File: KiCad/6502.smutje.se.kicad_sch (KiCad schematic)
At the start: 10 parts, among them U11 W65C02S

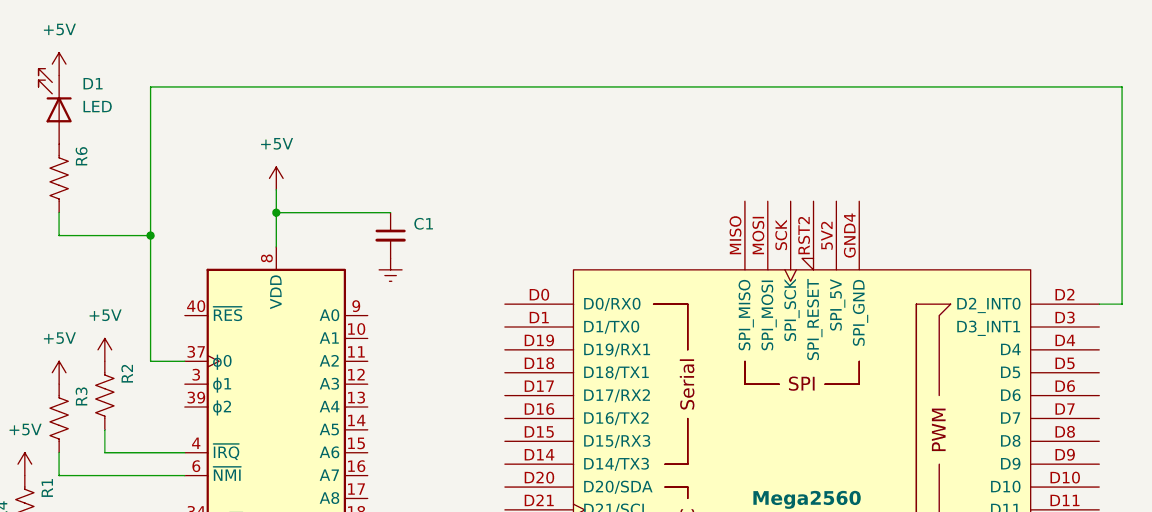
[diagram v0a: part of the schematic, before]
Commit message: Add trim potentiometer symbol and update power symbols in schematics
- Introduced a new trim potentiometer symbol (Device:R_Potentiometer_Trim) with properties for reference, value, footprint, and simulation details.
- Updated existing power symbols for +5V and Earth, including new references and descriptions.
- Adjusted positions and properties of various components in the schematic to enhance clarity and organization.
- Updated multiple schematic images to reflect the latest changes.
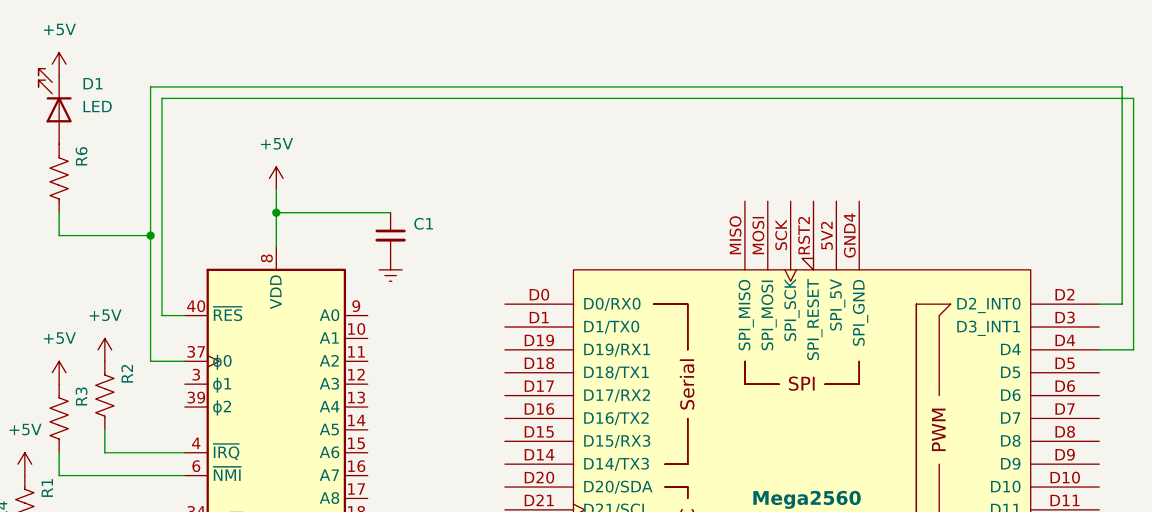
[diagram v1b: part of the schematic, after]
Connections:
- net at A5.D4: now also U11.40 (~{RES})
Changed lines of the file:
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@@
+	(wire
+		(pts
+			(xy 217.17 97.79) (xy 213.36 97.79)
+		)
+		(stroke
+			(width 0)
+			(type default)
+		)
+	)
 	(wire
 		(pts
@@
 	(wire
 		(pts
+			(xy 217.17 69.85) (xy 217.17 97.79)
+		)
+		(stroke
+			(width 0)
+			(type default)
+		)
+	)
+	(wire
+		(pts
+			(xy 111.76 93.98) (xy 109.22 93.98)
+		)
+		(stroke
+			(width 0)
+			(type default)
+		)
+	)
+	(wire
+		(pts
 			(xy 107.95 85.09) (xy 97.79 85.09)
 		)
@@
 	(wire
 		(pts
+			(xy 109.22 69.85) (xy 217.17 69.85)
+		)
+		(stroke
+			(width 0)
+			(type default)
+		)
+	)
+	(wire
+		(pts
 			(xy 97.79 109.22) (xy 97.79 111.76)
 		)
@@
 		)
 		(stroke
+			(width 0)
+			(type default)
+		)
+	)
+	(wire
+		(pts
+			(xy 109.22 93.98) (xy 109.22 69.85)
+		)
+		(stroke

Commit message: Revert "Add trim potentiometer symbol and update power symbols in schematics"
This reverts commit c4bb345892a428583a00d61d4c040ffcc3a1eb40.
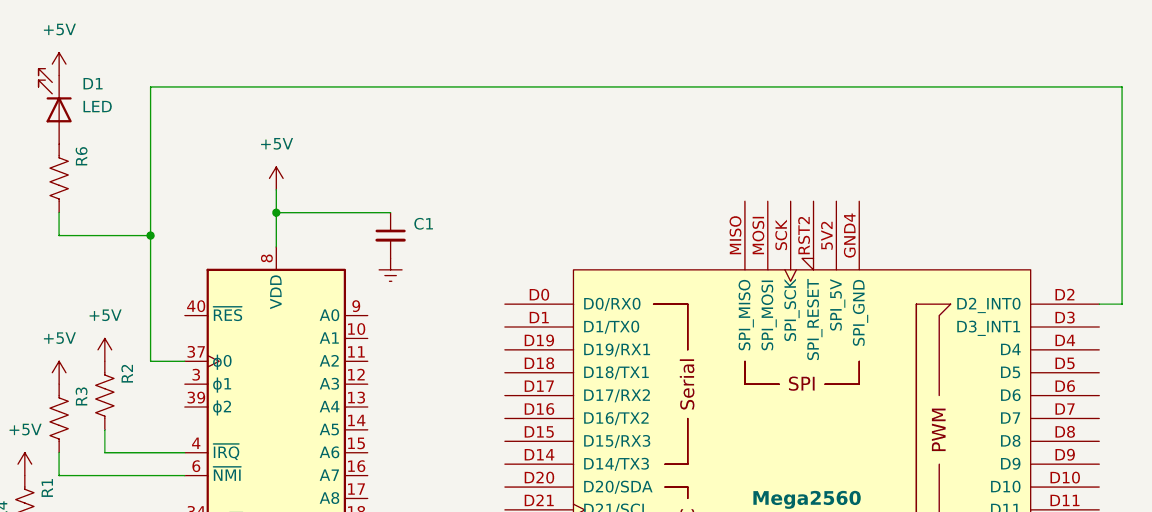
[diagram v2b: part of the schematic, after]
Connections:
- net at A5.D4: no longer U11.40 (~{RES})
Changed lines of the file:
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@@
-	(wire
-		(pts
-			(xy 217.17 97.79) (xy 213.36 97.79)
-		)
-		(stroke
-			(width 0)
-			(type default)
-		)
-	)
 	(wire
 		(pts
@@
 		(pts
 			(xy 121.92 82.55) (xy 121.92 86.36)
-		)
-		(stroke
-			(width 0)
-			(type default)
-		)
-	)
-	(wire
-		(pts
-			(xy 217.17 69.85) (xy 217.17 97.79)
-		)
-		(stroke
-			(width 0)
-			(type default)
-		)
-	)
-	(wire
-		(pts
-			(xy 111.76 93.98) (xy 109.22 93.98)
 		)
 		(stroke
@@
 		(pts
 			(xy 111.76 109.22) (xy 102.87 109.22)
-		)
-		(stroke
-			(width 0)
-			(type default)
-		)
-	)
-	(wire
-		(pts
-			(xy 109.22 69.85) (xy 217.17 69.85)
 		)
 		(stroke
@@
 		)
 		(stroke
-			(width 0)
-			(type default)
-		)
-	)
-	(wire
-		(pts
-			(xy 109.22 93.98) (xy 109.22 69.85)
-		)
-		(stroke
